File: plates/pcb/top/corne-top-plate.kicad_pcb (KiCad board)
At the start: 2 copper layers, 132.9 x 91.4 mm, 28 parts, among them SW2 KEY_SWITCH

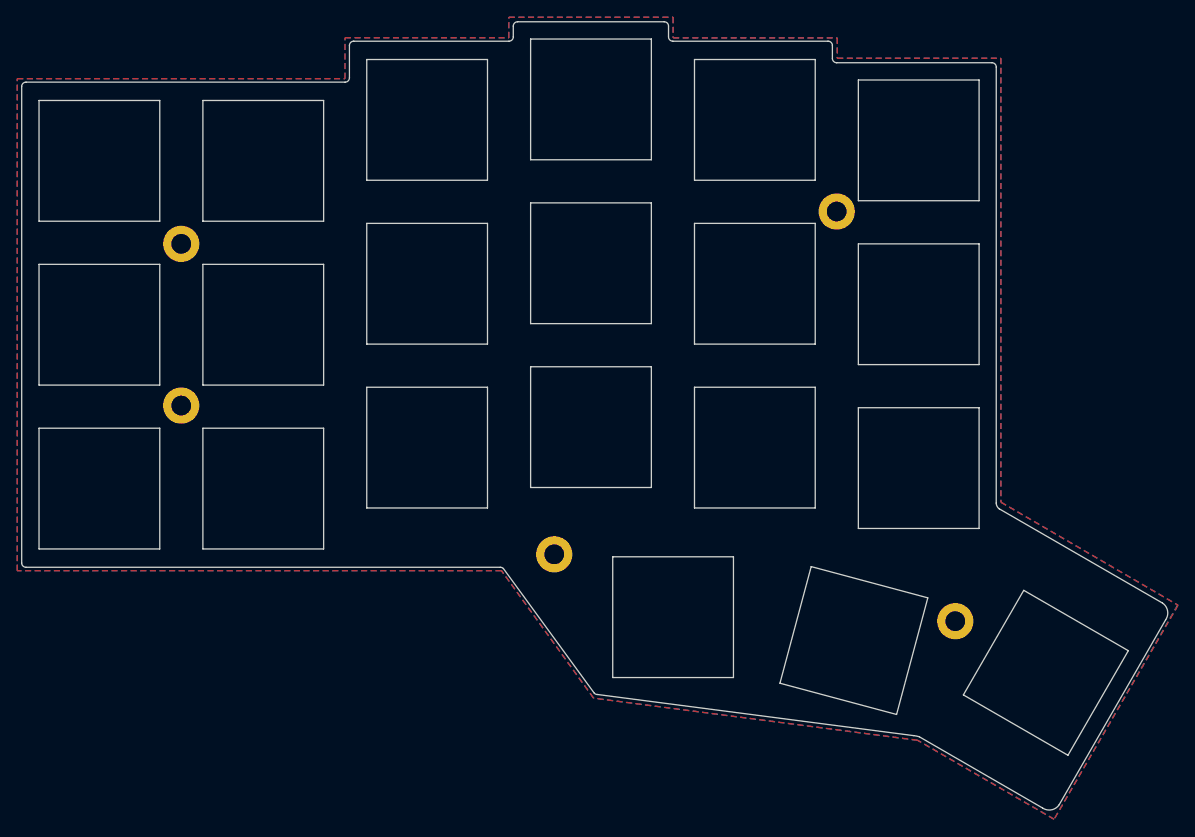
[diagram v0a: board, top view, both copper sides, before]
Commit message: modify ultralight with kailh hotswap
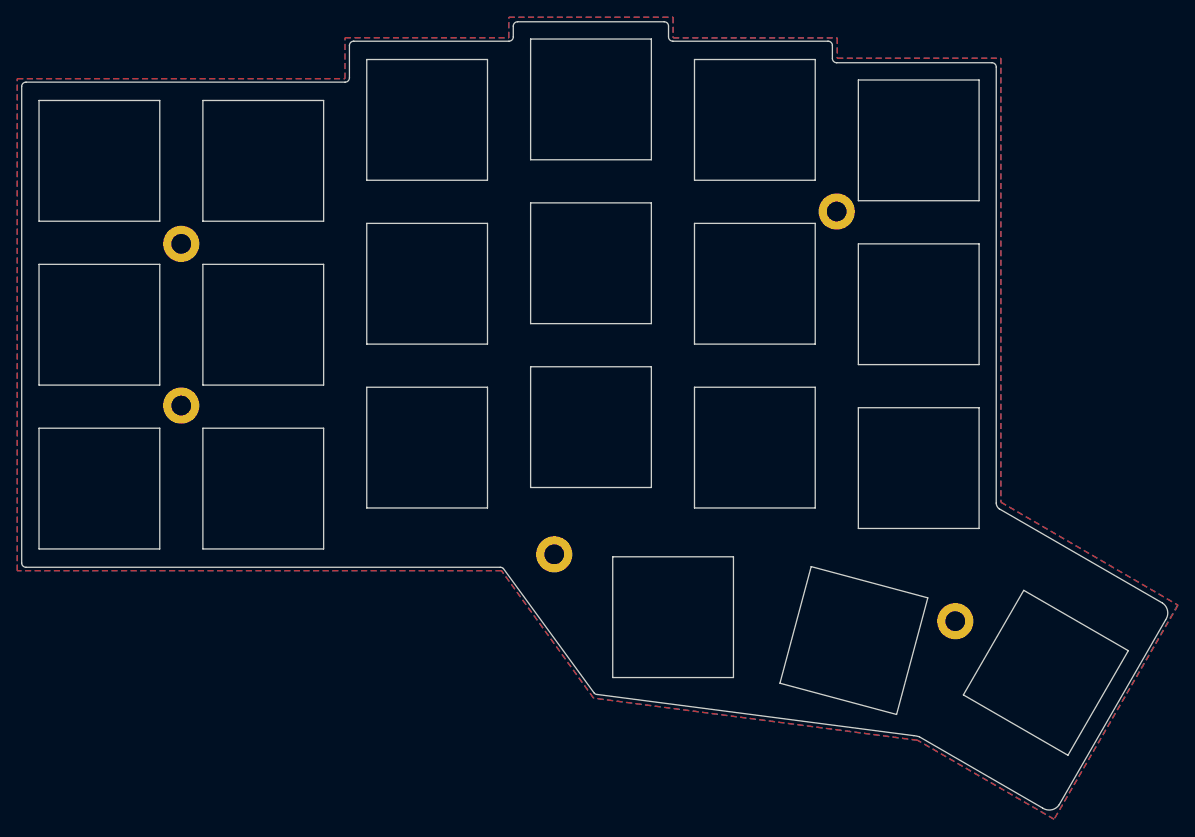
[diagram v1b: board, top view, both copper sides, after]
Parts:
- removed G*** (x2): LOGO, kbd:corne-logo-horizontal-mask
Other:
- net class Default removed
